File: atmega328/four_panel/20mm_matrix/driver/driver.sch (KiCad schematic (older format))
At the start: 20 parts, among them IC1 ATMEGA328-A, IC2 ATMEGA328-A, IC3 ATMEGA328-A, IC4 ATMEGA328-A, P1 CONN_2X2, P2 CONN_2X2, X1 CER_RESO, X2 CER_RESO, X3 CER_RESO, X4 CER_RESO

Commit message: Finished initial verision of four matrix atmega328 based design.
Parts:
- removed IC1, IC2, IC3, IC4: ATMEGA328-A, TQFP32, symbol ATMEGA328-A
- added C3, C4: 0.1uF, symbol C
- added IC1, IC2, IC3, IC4: ATMEGA328P-M, MLF/QFN32, symbol ATMEGA328P-M
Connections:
- wire segments 222 -> 230
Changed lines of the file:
@@
 $EndDescr
-$Comp
-L ATMEGA328-A IC1
-U 1 1 521285C1
-P 2400 3550
-F 0 "IC1" H 1650 4800 40  0000 L BNN
-F 1 "ATMEGA328-A" H 2800 2150 40  0000 L BNN
-F 2 "TQFP32" H 2400 3550 30  0000 C CIN
-F 3 "" H 2400 3550 60  0000 C CNN
-	1    2400 3550
-	1    0    0    -1
-$EndComp
 $Comp
 L CER_RESO X1
@@
 	1500 4550 1300 4550
 Wire Wire Line
-	1300 4550 1300 4950
+	1300 4450 1300 4950
 Wire Wire Line
 	1500 4650 1300 4650
@@
 RESET_DRV1
 $Comp
-L ATMEGA328-A IC2
-U 1 1 521296D4
-P 6700 3550
-F 0 "IC2" H 5950 4800 40  0000 L BNN
-F 1 "ATMEGA328-A" H 7100 2150 40  0000 L BNN
-F 2 "TQFP32" H 6700 3550 30  0000 C CIN
-F 3 "" H 6700 3550 60  0000 C CNN
-	1    6700 3550
-	1    0    0    -1
-$EndComp
-$Comp
 L CER_RESO X2
 U 1 1 521296DA
@@
 	5800 4550 5600 4550
 Wire Wire Line
-	5600 4550 5600 4950
+	5600 4450 5600 4950
 Wire Wire Line
 	5800 4650 5600 4650
@@
 	10200 4550 10000 4550
 Wire Wire Line
-	10000 4550 10000 4950
+	10000 4450 10000 4950
 Wire Wire Line
 	10200 4650 10000 4650
@@
 	14350 4550 14150 4550
 Wire Wire Line
-	14150 4550 14150 4950
+	14150 4450 14150 4950
 Wire Wire Line
 	14350 4650 14150 4650
@@
 Wire Wire Line
 	17350 900  17350 700
-$Comp
-L ATMEGA328-A IC3
-U 1 1 5213039D
-P 11100 3550
-F 0 "IC3" H 10350 4800 40  0000 L BNN
-F 1 "ATMEGA328-A" H 11500 2150 40  0000 L BNN
-F 2 "TQFP32" H 11100 3550 30  0000 C CIN
-F 3 "" H 11100 3550 60  0000 C CNN
-	1    11100 3550
-	1    0    0    -1
-$EndComp
-$Comp
-L ATMEGA328-A IC4
-U 1 1 521303AC
-P 15250 3550
-F 0 "IC4" H 14500 4800 40  0000 L BNN
-F 1 "ATMEGA328-A" H 15650 2150 40  0000 L BNN
-F 2 "TQFP32" H 15250 3550 30  0000 C CIN
-F 3 "" H 15250 3550 60  0000 C CNN
-	1    15250 3550
-	1    0    0    -1
-$EndComp
 Text Notes 7650 9050 0    100  ~ 0
 POWER FILTERING
@@
 Text Label 14350 6550 2    60   ~ 0
 ROW8_DRV4
+$Comp
+L ATMEGA328P-M IC1
+U 1 1 521524F8
+P 2400 3550
+F 0 "IC1" H 1700 4800 50  0000 L BNN
+F 1 "ATMEGA328P-M" H 2600 2150 50  0000 L BNN
+F 2 "MLF/QFN32" H 1950 2200 50  0001 C CNN
+F 3 "" H 2400 3550 60  0000 C CNN
+	1    2400 3550
+	1    0    0    -1
+$EndComp
+Wire Wire Line
+	1500 4450 1300 4450
+Connection ~ 1300 4550
+$Comp
+L ATMEGA328P-M IC2
+U 1 1 521527DA
+P 6700 3550
+F 0 "IC2" H 6000 4800 50  0000 L BNN
+F 1 "ATMEGA328P-M" H 6900 2150 50  0000 L BNN
+F 2 "MLF/QFN32" H 6250 2200 50  0001 C CNN
+F 3 "" H 6700 3550 60  0000 C CNN
+	1    6700 3550
+	1    0    0    -1
+$EndComp
+Wire Wire Line
+	5800 4450 5600 4450
+Connection ~ 5600 4550
+$Comp
+L ATMEGA328P-M IC3
+U 1 1 52152A7F
+P 11100 3550
+F 0 "IC3" H 10400 4800 50  0000 L BNN
+F 1 "ATMEGA328P-M" H 11300 2150 50  0000 L BNN
+F 2 "MLF/QFN32" H 10650 2200 50  0001 C CNN
+F 3 "" H 11100 3550 60  0000 C CNN
+	1    11100 3550
+	1    0    0    -1
+$EndComp
+Wire Wire Line
+	10200 4450 10000 4450
+Connection ~ 10000 4550
+$Comp
+L ATMEGA328P-M IC4
+U 1 1 52152D26
+P 15250 3550
+F 0 "IC4" H 14550 4800 50  0000 L BNN
+F 1 "ATMEGA328P-M" H 15450 2150 50  0000 L BNN
+F 2 "MLF/QFN32" H 14800 2200 50  0001 C CNN
+F 3 "" H 15250 3550 60  0000 C CNN
+	1    15250 3550
+	1    0    0    -1
+$EndComp
+Wire Wire Line
+	14350 4450 14150 4450
+Connection ~ 14150 4550
+$Comp
+L C C3
+U 1 1 521514DE
+P 8450 9700
+F 0 "C3" H 8450 9800 40  0000 L CNN
+F 1 "0.1uF" H 8456 9615 40  0000 L CNN
+F 2 "" H 8488 9550 30  0000 C CNN
+F 3 "" H 8450 9700 60  0000 C CNN
+	1    8450 9700
+	1    0    0    -1
+$EndComp
+$Comp
+L C C4
+U 1 1 521514E4
+P 8800 9700
+F 0 "C4" H 8800 9800 40  0000 L CNN
+F 1 "0.1uF" H 8806 9615 40  0000 L CNN
+F 2 "" H 8838 9550 30  0000 C CNN
+F 3 "" H 8800 9700 60  0000 C CNN
+	1    8800 9700
+	1    0    0    -1
+$EndComp
+$Comp
+L +5V #PWR027
+U 1 1 521514EA
+P 8450 9350
+F 0 "#PWR027" H 8450 9440 20  0001 C CNN
+F 1 "+5V" H 8450 9440 30  0000 C CNN
+F 2 "" H 8450 9350 60  0000 C CNN
+F 3 "" H 8450 9350 60  0000 C CNN
+	1    8450 9350
+	1    0    0    -1
+$EndComp
+$Comp
+L +5V #PWR028
+U 1 1 521514F0
+P 8800 9350
+F 0 "#PWR028" H 8800 9440 20  0001 C CNN
+F 1 "+5V" H 8800 9440 30  0000 C CNN
+F 2 "" H 8800 9350 60  0000 C CNN
+F 3 "" H 8800 9350 60  0000 C CNN
+	1    8800 9350
+	1    0    0    -1
+$EndComp
+$Comp
+L GND #PWR029
+U 1 1 521514F6
+P 8450 10050
+F 0 "#PWR029" H 8450 10050 30  0001 C CNN
+F 1 "GND" H 8450 9980 30  0001 C CNN
+F 2 "" H 8450 10050 60  0000 C CNN
+F 3 "" H 8450 10050 60  0000 C CNN
+	1    8450 10050
+	1    0    0    -1
+$EndComp
+$Comp
+L GND #PWR030
+U 1 1 521514FC
+P 8800 10050
+F 0 "#PWR030" H 8800 10050 30  0001 C CNN
+F 1 "GND" H 8800 9980 30  0001 C CNN
+F 2 "" H 8800 10050 60  0000 C CNN
+F 3 "" H 8800 10050 60  0000 C CNN
+	1    8800 10050
+	1    0    0    -1
+$EndComp
+Wire Wire Line
+	8450 9350 8450 9500
+Wire Wire Line
+	8800 9350 8800 9500
+Wire Wire Line
+	8450 9900 8450 10050
+Wire Wire Line
+	8800 9900 8800 10050
 $EndSCHEMATC

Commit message: Finished initial version of four matrix atmega328 based design.
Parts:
- added R10, R11, R12, R13, R14, R15, R16, R17, R18, R19, R20, R21, R22, R23, R24, R25, R26, R27, R28, R29, R30, R31, R32, R33, R34, R35, R36, R5, R6, R7, R8, R9: R, symbol R
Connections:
- net ROW1_DRV1: now also R5.1; no longer MATRIX1.13 (A1)
- net ROW1_DRV2: now also R13.1; no longer MATRIX2.13 (A1)
- net ROW1_DRV3: now also R21.1; no longer MATRIX3.13 (A1)
- net ROW1_DRV4: now also R29.1; no longer MATRIX4.13 (A1)
- net ROW2_DRV1: now also R6.1; no longer MATRIX1.3 (A2)
- net ROW2_DRV2: now also R14.1; no longer MATRIX2.3 (A2)
- net ROW2_DRV3: now also R22.1; no longer MATRIX3.3 (A2)
- net ROW2_DRV4: now also R30.1; no longer MATRIX4.3 (A2)
- net ROW3_DRV1: now also R7.1; no longer MATRIX1.4 (A3)
- net ROW3_DRV2: now also R15.1; no longer MATRIX2.4 (A3)
- net ROW3_DRV3: now also R23.1; no longer MATRIX3.4 (A3)
- net ROW3_DRV4: now also R31.1; no longer MATRIX4.4 (A3)
- net ROW4_DRV1: now also R8.1; no longer MATRIX1.10 (A4)
- net ROW4_DRV2: now also R16.1; no longer MATRIX2.10 (A4)
- net ROW4_DRV3: now also R24.1; no longer MATRIX3.10 (A4)
- net ROW4_DRV4: now also R32.1; no longer MATRIX4.10 (A4)
- net ROW5_DRV1: now also R9.1; no longer MATRIX1.6 (A5)
- net ROW5_DRV2: now also R17.1; no longer MATRIX2.6 (A5)
- net ROW5_DRV3: now also R25.1; no longer MATRIX3.6 (A5)
- net ROW5_DRV4: now also R33.1; no longer MATRIX4.6 (A5)
- net ROW6_DRV1: now also R10.1; no longer MATRIX1.11 (A6)
- net ROW6_DRV2: now also R18.1; no longer MATRIX2.11 (A6)
- net ROW6_DRV3: now also R26.1; no longer MATRIX3.11 (A6)
- net ROW6_DRV4: now also R34.1; no longer MATRIX4.11 (A6)
- net ROW7_DRV1: now also R11.1; no longer MATRIX1.15 (A7)
- net ROW7_DRV2: now also R19.1; no longer MATRIX2.15 (A7)
- net ROW7_DRV3: now also R27.1; no longer MATRIX3.15 (A7)
- net ROW7_DRV4: now also R35.1; no longer MATRIX4.15 (A7)
- net ROW8_DRV1: now also R12.1; no longer MATRIX1.16 (A8)
- net ROW8_DRV2: now also R20.1; no longer MATRIX2.16 (A8)
- net ROW8_DRV3: now also R28.1; no longer MATRIX3.16 (A8)
- net ROW8_DRV4: now also R36.1; no longer MATRIX4.16 (A8)
- new net: MATRIX2.10 (A4), R16.2
- new net: MATRIX2.11 (A6), R18.2
- new net: MATRIX2.13 (A1), R13.2
- new net: MATRIX2.15 (A7), R19.2
- new net: MATRIX2.16 (A8), R20.2
- new net: MATRIX2.3 (A2), R14.2
- new net: MATRIX2.4 (A3), R15.2
- new net: MATRIX2.6 (A5), R17.2
- new net: MATRIX3.10 (A4), R24.2
- new net: MATRIX3.11 (A6), R26.2
- new net: MATRIX3.13 (A1), R21.2
- new net: MATRIX3.15 (A7), R27.2
- new net: MATRIX3.16 (A8), R28.2
- new net: MATRIX3.3 (A2), R22.2
- new net: MATRIX3.4 (A3), R23.2
- new net: MATRIX3.6 (A5), R25.2
- new net: MATRIX4.10 (A4), R32.2
- new net: MATRIX4.11 (A6), R34.2
- new net: MATRIX4.13 (A1), R29.2
- new net: MATRIX4.15 (A7), R35.2
- new net: MATRIX4.16 (A8), R36.2
- new net: MATRIX4.3 (A2), R30.2
- new net: MATRIX4.4 (A3), R31.2
- new net: MATRIX4.6 (A5), R33.2
- new net: MATRIX1.10 (A4), R8.2
- new net: MATRIX1.11 (A6), R10.2
- new net: MATRIX1.13 (A1), R5.2
- new net: MATRIX1.15 (A7), R11.2
- new net: MATRIX1.16 (A8), R12.2
- new net: MATRIX1.3 (A2), R6.2
- new net: MATRIX1.4 (A3), R7.2
- new net: MATRIX1.6 (A5), R9.2
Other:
- note added: "LED Matrices"
- moved on the sheet: C1, C2, C3, C4, MATRIX1, MATRIX2, MATRIX3, MATRIX4, P1, P2

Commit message: Modified 4 matrix atmega328 design. Added pin change interrupts and re-routed.
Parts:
- removed P1, P2: CONN_2X2, symbol CONN_2X2
- added P1, P2: CONN_3X2, symbol CONN_3X2
- R10, R11, R12, R13, R14, R15, R16, R17, R18, R19, R20, R21, R22, R23, R24, R25, R26, R27, R28, R29, R30, R31, R32, R33, R34, R35, R36, R5, R6, R7, R8, R9: value R -> 180
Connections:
- net +5V: now also P1.1
- net GND: now also P1.3
- net RESET_DRV1: now also P1.2
- net RESET_DRV2: now also P1.4
- net RESET_DRV3: now also P2.2
- net RESET_DRV4: now also P2.4
- net SCL: now also P2.3
- net SDA: now also P2.1
- net PCINT10/PC2: now reaches IC1.25 ((PCINT10/ADC2)PC2)
- net PCINT10/PC2: now also IC2.25 ((PCINT10/ADC2)PC2), IC3.25 ((PCINT10/ADC2)PC2), IC4.25 ((PCINT10/ADC2)PC2), P1.6
- net PCINT11/PC3: now reaches IC1.26 ((PCINT11/ADC3)PC3)
- net PCINT11/PC3: now also IC2.26 ((PCINT11/ADC3)PC3), IC3.26 ((PCINT11/ADC3)PC3), IC4.26 ((PCINT11/ADC3)PC3), P2.5
- no-connect marks 16 -> 10
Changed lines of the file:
@@
 Text Label 3650 4750 0    60   ~ 0
 COL8_DRV1
-NoConn ~ 3400 3500
-NoConn ~ 3400 3600
 $Comp
 L +5V #PWR04
@@
 Text Label 7950 4750 0    60   ~ 0
 COL8_DRV2
-NoConn ~ 7700 3500
-NoConn ~ 7700 3600
 $Comp
 L +5V #PWR08
@@
 Text Label 12350 4750 0    60   ~ 0
 COL8_DRV3
-NoConn ~ 12100 3500
-NoConn ~ 12100 3600
 $Comp
 L +5V #PWR012
@@
 Text Label 16500 4750 0    60   ~ 0
 COL8_DRV4
-NoConn ~ 16250 3500
-NoConn ~ 16250 3600
 $Comp
 L +5V #PWR016
@@
 Wire Wire Line
 	9550 13100 9550 13250
-$Comp
-L CONN_2X2 P1
-U 1 1 5213131F
-P 1850 12900
-F 0 "P1" H 1850 13050 50  0000 C CNN
-F 1 "CONN_2X2" H 1860 12770 40  0000 C CNN
-F 2 "" H 1850 12900 60  0000 C CNN
-F 3 "" H 1850 12900 60  0000 C CNN
-	1    1850 12900
-	1    0    0    -1
-$EndComp
-$Comp
-L CONN_2X2 P2
-U 1 1 5213132E
-P 4250 12900
-F 0 "P2" H 4250 13050 50  0000 C CNN
-F 1 "CONN_2X2" H 4260 12770 40  0000 C CNN
-F 2 "" H 4250 12900 60  0000 C CNN
-F 3 "" H 4250 12900 60  0000 C CNN
-	1    4250 12900
-	1    0    0    -1
-$EndComp
 Wire Wire Line
 	1050 12850 1450 12850
@@
 	2250 12950 2500 12950
 Wire Wire Line
-	3850 12850 3600 12850
-Wire Wire Line
-	3850 12950 3600 12950
-Wire Wire Line
-	4650 12850 4900 12850
-Wire Wire Line
-	4650 12950 4900 12950
+	4100 12850 3850 12850
+Wire Wire Line
+	4100 12950 3850 12950
+Wire Wire Line
+	4900 12850 5150 12850
+Wire Wire Line
+	4900 12950 5150 12950
 $Comp
 L +5V #PWR025
@@
 Text Label 2500 12950 0    60   ~ 0
 RESET_DRV2
-Text Label 3600 12850 2    60   ~ 0
+Text Label 3850 12850 2    60   ~ 0
 SDA
-Text Label 3600 12950 2    60   ~ 0
+Text Label 3850 12950 2    60   ~ 0
 SCL
-Text Label 4900 12850 0    60   ~ 0
+Text Label 5150 12850 0    60   ~ 0
 RESET_DRV3
-Text Label 4900 12950 0    60   ~ 0
+Text Label 5150 12950 0    60   ~ 0
 RESET_DRV4
 Text Notes 4300 12350 2    100  ~ 0
@@
 P 2300 7350
 F 0 "R6" V 2380 7350 40  0000 C CNN
-F 1 "R" V 2307 7351 40  0000 C CNN
+F 1 "180" V 2307 7351 40  0000 C CNN
 F 2 "" V 2230 7350 30  0000 C CNN
 F 3 "" H 2300 7350 30  0000 C CNN
@@
 P 2500 7350
 F 0 "R7" V 2580 7350 40  0000 C CNN
-F 1 "R" V 2507 7351 40  0000 C CNN
+F 1 "180" V 2507 7351 40  0000 C CNN
 F 2 "" V 2430 7350 30  0000 C CNN
 F 3 "" H 2500 7350 30  0000 C CNN
@@
 P 2100 7350
 F 0 "R5" V 2180 7350 40  0000 C CNN
-F 1 "R" V 2107 7351 40  0000 C CNN
+F 1 "180" V 2107 7351 40  0000 C CNN
 F 2 "" V 2030 7350 30  0000 C CNN
 F 3 "" H 2100 7350 30  0000 C CNN
@@
 P 2700 7350
 F 0 "R8" V 2780 7350 40  0000 C CNN
-F 1 "R" V 2707 7351 40  0000 C CNN
+F 1 "180" V 2707 7351 40  0000 C CNN
 F 2 "" V 2630 7350 30  0000 C CNN
 F 3 "" H 2700 7350 30  0000 C CNN
@@
 P 2900 7350
 F 0 "R9" V 2980 7350 40  0000 C CNN
-F 1 "R" V 2907 7351 40  0000 C CNN
+F 1 "180" V 2907 7351 40  0000 C CNN
 F 2 "" V 2830 7350 30  0000 C CNN
 F 3 "" H 2900 7350 30  0000 C CNN
@@
 P 3100 7350
 F 0 "R10" V 3180 7350 40  0000 C CNN
-F 1 "R" V 3107 7351 40  0000 C CNN
+F 1 "180" V 3107 7351 40  0000 C CNN
 F 2 "" V 3030 7350 30  0000 C CNN
 F 3 "" H 3100 7350 30  0000 C CNN
@@
 P 3300 7350
 F 0 "R11" V 3380 7350 40  0000 C CNN
-F 1 "R" V 3307 7351 40  0000 C CNN
+F 1 "180" V 3307 7351 40  0000 C CNN
 F 2 "" V 3230 7350 30  0000 C CNN
 F 3 "" H 3300 7350 30  0000 C CNN
@@
 P 3500 7350
 F 0 "R12" V 3580 7350 40  0000 C CNN
-F 1 "R" V 3507 7351 40  0000 C CNN
+F 1 "180" V 3507 7351 40  0000 C CNN
 F 2 "" V 3430 7350 30  0000 C CNN
 F 3 "" H 3500 7350 30  0000 C CNN
@@
 P 6800 7350
 F 0 "R14" V 6880 7350 40  0000 C CNN
-F 1 "R" V 6807 7351 40  0000 C CNN
+F 1 "180" V 6807 7351 40  0000 C CNN
 F 2 "" V 6730 7350 30  0000 C CNN
 F 3 "" H 6800 7350 30  0000 C CNN
@@
 P 7000 7350
 F 0 "R15" V 7080 7350 40  0000 C CNN
-F 1 "R" V 7007 7351 40  0000 C CNN
+F 1 "180" V 7007 7351 40  0000 C CNN
 F 2 "" V 6930 7350 30  0000 C CNN
 F 3 "" H 7000 7350 30  0000 C CNN
@@
 P 6600 7350
 F 0 "R13" V 6680 7350 40  0000 C CNN
-F 1 "R" V 6607 7351 40  0000 C CNN
+F 1 "180" V 6607 7351 40  0000 C CNN
 F 2 "" V 6530 7350 30  0000 C CNN
 F 3 "" H 6600 7350 30  0000 C CNN
@@
 P 7200 7350
 F 0 "R16" V 7280 7350 40  0000 C CNN
-F 1 "R" V 7207 7351 40  0000 C CNN
+F 1 "180" V 7207 7351 40  0000 C CNN
 F 2 "" V 7130 7350 30  0000 C CNN
 F 3 "" H 7200 7350 30  0000 C CNN
@@
 P 7400 7350
 F 0 "R17" V 7480 7350 40  0000 C CNN
-F 1 "R" V 7407 7351 40  0000 C CNN
+F 1 "180" V 7407 7351 40  0000 C CNN
 F 2 "" V 7330 7350 30  0000 C CNN
 F 3 "" H 7400 7350 30  0000 C CNN
@@
 P 7600 7350
 F 0 "R18" V 7680 7350 40  0000 C CNN
-F 1 "R" V 7607 7351 40  0000 C CNN
+F 1 "180" V 7607 7351 40  0000 C CNN
 F 2 "" V 7530 7350 30  0000 C CNN
 F 3 "" H 7600 7350 30  0000 C CNN
@@
 P 7800 7350
 F 0 "R19" V 7880 7350 40  0000 C CNN
-F 1 "R" V 7807 7351 40  0000 C CNN
+F 1 "180" V 7807 7351 40  0000 C CNN
 F 2 "" V 7730 7350 30  0000 C CNN
 F 3 "" H 7800 7350 30  0000 C CNN
@@
 P 8000 7350
 F 0 "R20" V 8080 7350 40  0000 C CNN
-F 1 "R" V 8007 7351 40  0000 C CNN
+F 1 "180" V 8007 7351 40  0000 C CNN
 F 2 "" V 7930 7350 30  0000 C CNN
 F 3 "" H 8000 7350 30  0000 C CNN
@@
 P 11150 7350
 F 0 "R22" V 11230 7350 40  0000 C CNN
-F 1 "R" V 11157 7351 40  0000 C CNN
+F 1 "180" V 11157 7351 40  0000 C CNN
 F 2 "" V 11080 7350 30  0000 C CNN
 F 3 "" H 11150 7350 30  0000 C CNN
@@
 P 11350 7350
 F 0 "R23" V 11430 7350 40  0000 C CNN
-F 1 "R" V 11357 7351 40  0000 C CNN
+F 1 "180" V 11357 7351 40  0000 C CNN
 F 2 "" V 11280 7350 30  0000 C CNN
 F 3 "" H 11350 7350 30  0000 C CNN
@@
 P 10950 7350
 F 0 "R21" V 11030 7350 40  0000 C CNN
-F 1 "R" V 10957 7351 40  0000 C CNN
+F 1 "180" V 10957 7351 40  0000 C CNN
 F 2 "" V 10880 7350 30  0000 C CNN
 F 3 "" H 10950 7350 30  0000 C CNN
@@
 P 11550 7350
 F 0 "R24" V 11630 7350 40  0000 C CNN
-F 1 "R" V 11557 7351 40  0000 C CNN
+F 1 "180" V 11557 7351 40  0000 C CNN
 F 2 "" V 11480 7350 30  0000 C CNN
 F 3 "" H 11550 7350 30  0000 C CNN
@@
 P 11750 7350
 F 0 "R25" V 11830 7350 40  0000 C CNN
-F 1 "R" V 11757 7351 40  0000 C CNN
+F 1 "180" V 11757 7351 40  0000 C CNN
 F 2 "" V 11680 7350 30  0000 C CNN
 F 3 "" H 11750 7350 30  0000 C CNN
@@
 P 11950 7350
 F 0 "R26" V 12030 7350 40  0000 C CNN
-F 1 "R" V 11957 7351 40  0000 C CNN
+F 1 "180" V 11957 7351 40  0000 C CNN
 F 2 "" V 11880 7350 30  0000 C CNN
 F 3 "" H 11950 7350 30  0000 C CNN
@@
 P 12150 7350
 F 0 "R27" V 12230 7350 40  0000 C CNN
-F 1 "R" V 12157 7351 40  0000 C CNN
+F 1 "180" V 12157 7351 40  0000 C CNN
 F 2 "" V 12080 7350 30  0000 C CNN
 F 3 "" H 12150 7350 30  0000 C CNN
@@
 P 12350 7350
 F 0 "R28" V 12430 7350 40  0000 C CNN
-F 1 "R" V 12357 7351 40  0000 C CNN
+F 1 "180" V 12357 7351 40  0000 C CNN
 F 2 "" V 12280 7350 30  0000 C CNN
 F 3 "" H 12350 7350 30  0000 C CNN
@@
 P 15250 7350
 F 0 "R30" V 15330 7350 40  0000 C CNN
-F 1 "R" V 15257 7351 40  0000 C CNN
+F 1 "180" V 15257 7351 40  0000 C CNN
 F 2 "" V 15180 7350 30  0000 C CNN
 F 3 "" H 15250 7350 30  0000 C CNN
@@
 P 15450 7350
 F 0 "R31" V 15530 7350 40  0000 C CNN
-F 1 "R" V 15457 7351 40  0000 C CNN
+F 1 "180" V 15457 7351 40  0000 C CNN
 F 2 "" V 15380 7350 30  0000 C CNN
 F 3 "" H 15450 7350 30  0000 C CNN
@@
 P 15050 7350
 F 0 "R29" V 15130 7350 40  0000 C CNN
-F 1 "R" V 15057 7351 40  0000 C CNN
+F 1 "180" V 15057 7351 40  0000 C CNN
 F 2 "" V 14980 7350 30  0000 C CNN
 F 3 "" H 15050 7350 30  0000 C CNN
@@
 P 15650 7350
 F 0 "R32" V 15730 7350 40  0000 C CNN
-F 1 "R" V 15657 7351 40  0000 C CNN
+F 1 "180" V 15657 7351 40  0000 C CNN
 F 2 "" V 15580 7350 30  0000 C CNN
 F 3 "" H 15650 7350 30  0000 C CNN
@@
 P 15850 7350
 F 0 "R33" V 15930 7350 40  0000 C CNN
-F 1 "R" V 15857 7351 40  0000 C CNN
+F 1 "180" V 15857 7351 40  0000 C CNN
 F 2 "" V 15780 7350 30  0000 C CNN
 F 3 "" H 15850 7350 30  0000 C CNN
@@
 P 16050 7350
 F 0 "R34" V 16130 7350 40  0000 C CNN
-F 1 "R" V 16057 7351 40  0000 C CNN
+F 1 "180" V 16057 7351 40  0000 C CNN
 F 2 "" V 15980 7350 30  0000 C CNN
 F 3 "" H 16050 7350 30  0000 C CNN
@@
 P 16250 7350
 F 0 "R35" V 16330 7350 40  0000 C CNN
-F 1 "R" V 16257 7351 40  0000 C CNN
+F 1 "180" V 16257 7351 40  0000 C CNN
 F 2 "" V 16180 7350 30  0000 C CNN
 F 3 "" H 16250 7350 30  0000 C CNN
@@
 P 16450 7350
 F 0 "R36" V 16530 7350 40  0000 C CNN
-F 1 "R" V 16457 7351 40  0000 C CNN
+F 1 "180" V 16457 7351 40  0000 C CNN
 F 2 "" V 16380 7350 30  0000 C CNN
 F 3 "" H 16450 7350 30  0000 C CNN
@@
 Wire Notes Line
 	600  12000 18450 12000
+Wire Wire Line
+	3400 3600 3650 3600
+Wire Wire Line
+	3400 3500 3650 3500
+Wire Wire Line
+	7700 3600 7950 3600
+Wire Wire Line
+	7700 3500 7950 3500
+Wire Wire Line
+	12100 3600 12350 3600
+Wire Wire Line
+	12100 3500 12350 3500
+Wire Wire Line
+	16250 3600 16500 3600
+Wire Wire Line
+	16250 3500 16500 3500
+Text Label 3650 3500 0    60   ~ 0
+PCINT10/PC2
+Text Label 3650 3600 0    60   ~ 0
+PCINT11/PC3
+Text Label 7950 3600 0    60   ~ 0
+PCINT11/PC3
+Text Label 7950 3500 0    60   ~ 0
+PCINT10/PC2
+Text Label 12350 3600 0    60   ~ 0
+PCINT11/PC3
+Text Label 12350 3500 0    60   ~ 0
+PCINT10/PC2
+Text Label 16500 3600 0    60   ~ 0
+PCINT11/PC3
+Text Label 16500 3500 0    60   ~ 0
+PCINT10/PC2
+$Comp
+L CONN_3X2 P1
+U 1 1 521A98BD
+P 1850 13000
+F 0 "P1" H 1850 13250 50  0000 C CNN
+F 1 "CONN_3X2" V 1850 13050 40  0000 C CNN
+F 2 "" H 1850 13000 60  0000 C CNN
+F 3 "" H 1850 13000 60  0000 C CNN
+	1    1850 13000
+	1    0    0    -1
+$EndComp
+$Comp
+L CONN_3X2 P2
+U 1 1 521A98CC
+P 4500 13000
+F 0 "P2" H 4500 13250 50  0000 C CNN
+F 1 "CONN_3X2" V 4500 13050 40  0000 C CNN
+F 2 "" H 4500 13000 60  0000 C CNN
+F 3 "" H 4500 13000 60  0000 C CNN
+	1    4500 13000
+	1    0    0    -1
+$EndComp
+NoConn ~ 4900 13050
+Wire Wire Line
+	4100 13050 3850 13050
+Wire Wire Line
+	2250 13050 2500 13050
+NoConn ~ 1450 13050
+Text Label 2500 13050 0    60   ~ 0
+PCINT10/PC2
+Text Label 3850 13050 2    60   ~ 0
+PCINT11/PC3
 $EndSCHEMATC

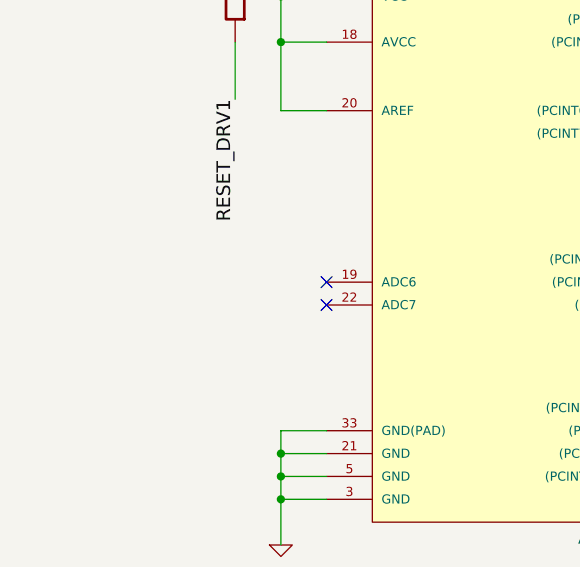
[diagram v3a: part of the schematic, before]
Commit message: Added svg and pdf of 4x20mm atmega328 test arena.
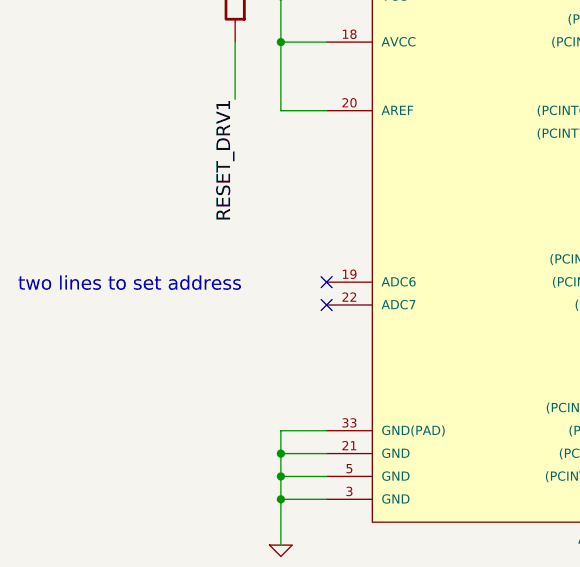
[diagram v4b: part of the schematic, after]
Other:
- note added: "two lines to set address"
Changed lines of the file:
@@
 Text Label 3850 13050 2    60   ~ 0
 PCINT11/PC3
+Text Notes 150  3850 0    60   ~ 0
+two lines to set address
 $EndSCHEMATC
